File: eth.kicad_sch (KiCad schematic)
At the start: 44 parts, among them J5 Bus_RJ45_5-2337992-8, Q4 DTC014T_SOT-416, Q5 DTC014T_SOT-416, U30 DP83867CR_VQFN, Y6 Oscillator_SMD_25MHz_ECS-2016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

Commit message: [#56935] Update symbol/footprint links; Migrate to KiCad 7
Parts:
- C100, C101, C102, C103, C104, C105, C106, C107, C108, C239, C240, C99: footprint kria-k26-devboard-footprints:C_0402_1005Metric -> antmicro-footprints:C_0402_1005Metric; symbol kria-k26-devboard:C_100n_0402 -> antmicroCapacitors0402:C_100n_0402
- C109, C110, C111, C112, C94, C95, C96, C97, C98: footprint kria-k26-devboard-footprints:C_0402_1005Metric -> antmicro-footprints:C_0402_1005Metric; symbol kria-k26-devboard:C_1u_0402 -> antmicroCapacitors0402:C_1u_0402
- C113, C92, C93: footprint kria-k26-devboard-footprints:C_0402_1005Metric -> antmicro-footprints:C_0402_1005Metric; symbol kria-k26-devboard:C_10n_0402 -> antmicroCapacitors0402:C_10n_0402
- C114, C90, C91: footprint kria-k26-devboard-footprints:C_0603_1608Metric -> antmicro-footprints:C_0603_1608Metric; symbol kria-k26-devboard:C_10u_0603 -> antmicroCapacitors0603:C_10u_0603
- J5: footprint kria-k26-devboard-footprints:RJ45_5-2337992-8_Horizontal -> antmicro-footprints:RJ45_5-2337992-8_Horizontal; symbol kria-k26-devboard:Bus_RJ45_5-2337992-8 -> antmicroModularConnectorsJacksWithMagnetics:Bus_RJ45_5-2337992-8
- Q4, Q5: footprint kria-k26-devboard-footprints:SOT-416 -> antmicro-footprints:SOT-416; symbol kria-k26-devboard:DTC014T_SOT-416 -> antmicroTransistorsBipolarSingle:DTC014T_SOT-416
- R67: footprint kria-k26-devboard-footprints:R_0402_1005Metric -> antmicro-footprints:R_0402_1005Metric; symbol kria-k26-devboard:R_10k_0402 -> antmicroResistors0402:R_10k_0402
- R68, R70: footprint kria-k26-devboard-footprints:R_0402_1005Metric -> antmicro-footprints:R_0402_1005Metric; symbol kria-k26-devboard:R_2k49_0402 -> antmicroResistors0402:R_2k49_0402
- R69: footprint kria-k26-devboard-footprints:R_0402_1005Metric -> antmicro-footprints:R_0402_1005Metric; symbol kria-k26-devboard:R_5k76_0402 -> antmicroResistors0402:R_5k76_0402
- R71, R76: footprint kria-k26-devboard-footprints:R_0402_1005Metric -> antmicro-footprints:R_0402_1005Metric; symbol kria-k26-devboard:R_2k2_0402 -> antmicroResistors0402:R_2k2_0402
- R72: footprint kria-k26-devboard-footprints:R_0402_1005Metric -> antmicro-footprints:R_0402_1005Metric; symbol kria-k26-devboard:R_11k_0402 -> antmicroResistors0402:R_11k_0402
- R73, R74, R75: footprint kria-k26-devboard-footprints:R_0402_1005Metric -> antmicro-footprints:R_0402_1005Metric; symbol kria-k26-devboard:R_4k7_0402 -> antmicroResistors0402:R_4k7_0402
- R77, R78: footprint kria-k26-devboard-footprints:R_0402_1005Metric -> antmicro-footprints:R_0402_1005Metric; symbol kria-k26-devboard:R_330R_0402 -> antmicroResistors0402:R_330R_0402
- U30: footprint kria-k26-devboard-footprints:QFN-48-1EP_7x7mm -> antmicro-footprints:QFN-48-1EP_7x7mm; symbol kria-k26-devboard:DP83867CR_VQFN -> antmicroInterfaceControllers:DP83867CR_VQFN
- Y6: footprint kria-k26-devboard-footprints:Oscillator_SMD_ECS_2016MV_2x1.6x0.85mm -> antmicro-footprints:Oscillator_SMD_ECS_2016MV_2x1.6x0.85mm; symbol kria-k26-devboard:Oscillator_SMD_25MHz_ECS-2016MV -> antmicroOscillators:Oscillator_25MHz_ESC_2016MV

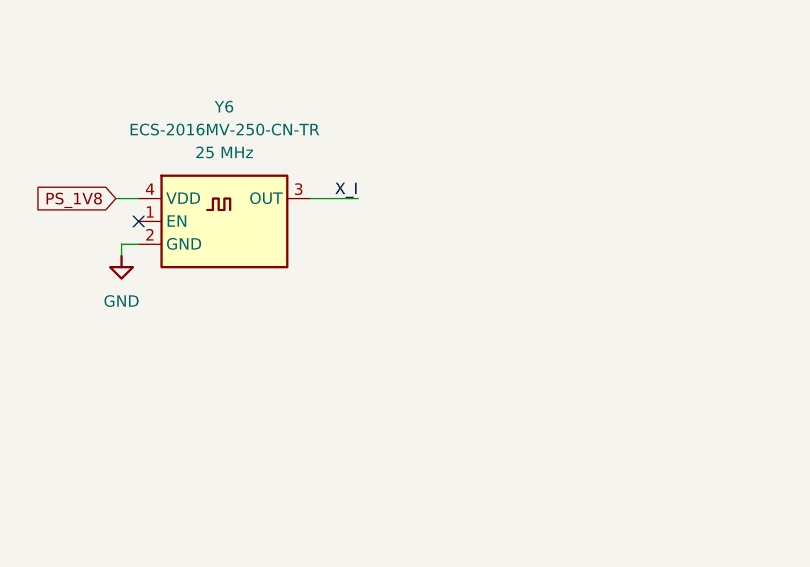
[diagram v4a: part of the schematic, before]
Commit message: [#56935] Fix missing highlights in OHP
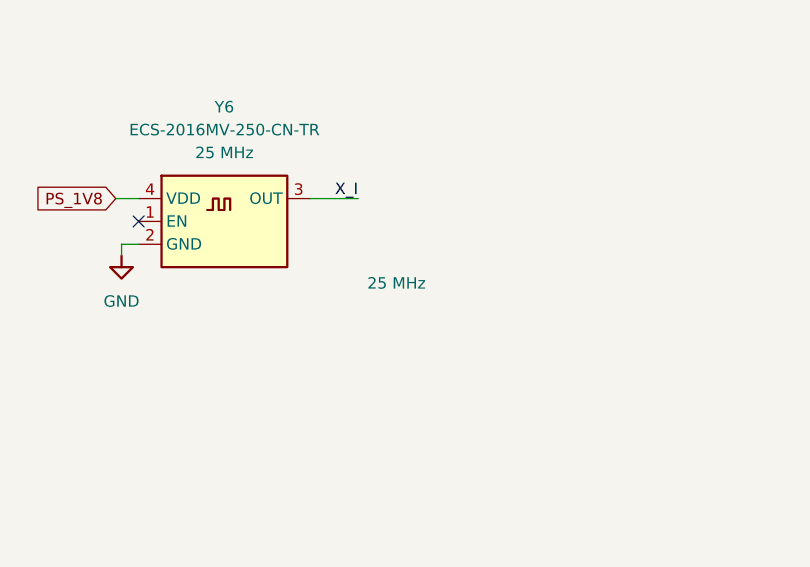
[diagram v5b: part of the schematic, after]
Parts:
- J5: VSD_Class (none) -> Ethernet
- Y6: value Oscillator_SMD_25MHz_ECS-2016MV -> Oscillator_25MHz_ESC_2016MV; Manufacturer ECS Inc. -> ECS Inc. International; Val (none) -> 25 MHz
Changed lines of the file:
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@@
       (effects (font (size 1.27 1.27) (thickness 0.15)) (justify left bottom) hide)
+    )
+    (property "VSD_Class" "Ethernet" (at 285.75 101.6 0)
+      (effects (font (size 1.27 1.27)) (justify left bottom) hide)
     )
     (pin "1")
@@
       (effects (font (size 1.27 1.27)))
     )
-    (property "Value" "Oscillator_SMD_25MHz_ECS-2016MV" (at 122.555 212.725 0)
+    (property "Value" "Oscillator_25MHz_ESC_2016MV" (at 122.555 212.725 0)
       (effects (font (size 1.27 1.27) (thickness 0.15)) hide)
     )
@@
       (effects (font (size 1.27 1.27) (thickness 0.15)) (justify left bottom) hide)
     )
-    (property "Datasheet" "https://www.mouser.pl/datasheet/2/122/ECS_2016MV-2529299.pdf" (at 108.585 217.17 0)
-      (effects (font (size 1.27 1.27) (thickness 0.15)) (justify left bottom) hide)
-    )
-    (property "Manufacturer" "ECS Inc." (at 116.84 231.775 0)
+    (property "Datasheet" "https://ecsxtal.com/store/pdf/ECS-2016MV.pdf" (at 108.585 217.17 0)
+      (effects (font (size 1.27 1.27) (thickness 0.15)) (justify left bottom) hide)
+    )
+    (property "Manufacturer" "ECS Inc. International" (at 116.84 231.775 0)
       (effects (font (size 1.27 1.27) (thickness 0.15)) (justify left bottom) hide)
     )
@@
       (effects (font (size 1.27 1.27) (thickness 0.15)))
     )
-    (pin "1")
+    (property "Val" "25 MHz" (at 138.43 230.505 0)
+      (effects (font (size 1.27 1.27) (thickness 0.15)) (justify left bottom))
+    )
+    (pin "1")

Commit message: [#56935] Loclib
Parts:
- C100, C101, C102, C103, C104, C105, C106, C107, C108, C239, C240, C99: footprint antmicro-footprints:C_0402_1005Metric -> kria-k26-devboard-footprints:C_0402_1005Metric; symbol antmicroCapacitors0402:C_100n_0402 -> kria-k26-devboard:C_100n_0402
- C109, C110, C111, C112, C94, C95, C96, C97, C98: footprint antmicro-footprints:C_0402_1005Metric -> kria-k26-devboard-footprints:C_0402_1005Metric; symbol antmicroCapacitors0402:C_1u_0402 -> kria-k26-devboard:C_1u_0402
- C113, C92, C93: footprint antmicro-footprints:C_0402_1005Metric -> kria-k26-devboard-footprints:C_0402_1005Metric; symbol antmicroCapacitors0402:C_10n_0402 -> kria-k26-devboard:C_10n_0402
- C114, C90, C91: footprint antmicro-footprints:C_0603_1608Metric -> kria-k26-devboard-footprints:C_0603_1608Metric; symbol antmicroCapacitors0603:C_10u_0603 -> kria-k26-devboard:C_10u_0603
- J5: footprint antmicro-footprints:RJ45_5-2337992-8_Horizontal -> kria-k26-devboard-footprints:RJ45_5-2337992-8_Horizontal; symbol antmicroModularConnectorsJacksWithMagnetics:Bus_RJ45_5-2337992-8 -> kria-k26-devboard:Bus_RJ45_5-2337992-8
- Q4, Q5: footprint antmicro-footprints:SOT-416 -> kria-k26-devboard-footprints:SOT-416; symbol antmicroTransistorsBipolarSingle:DTC014T_SOT-416 -> kria-k26-devboard:DTC014T_SOT-416
- R67: footprint antmicro-footprints:R_0402_1005Metric -> kria-k26-devboard-footprints:R_0402_1005Metric; symbol antmicroResistors0402:R_10k_0402 -> kria-k26-devboard:R_10k_0402
- R68, R70: footprint antmicro-footprints:R_0402_1005Metric -> kria-k26-devboard-footprints:R_0402_1005Metric; symbol antmicroResistors0402:R_2k49_0402 -> kria-k26-devboard:R_2k49_0402
- R69: footprint antmicro-footprints:R_0402_1005Metric -> kria-k26-devboard-footprints:R_0402_1005Metric; symbol antmicroResistors0402:R_5k76_0402 -> kria-k26-devboard:R_5k76_0402
- R71, R76: footprint antmicro-footprints:R_0402_1005Metric -> kria-k26-devboard-footprints:R_0402_1005Metric; symbol antmicroResistors0402:R_2k2_0402 -> kria-k26-devboard:R_2k2_0402
- R72: footprint antmicro-footprints:R_0402_1005Metric -> kria-k26-devboard-footprints:R_0402_1005Metric; symbol antmicroResistors0402:R_11k_0402 -> kria-k26-devboard:R_11k_0402
- R73, R74, R75: footprint antmicro-footprints:R_0402_1005Metric -> kria-k26-devboard-footprints:R_0402_1005Metric; symbol antmicroResistors0402:R_4k7_0402 -> kria-k26-devboard:R_4k7_0402
- R77, R78: footprint antmicro-footprints:R_0402_1005Metric -> kria-k26-devboard-footprints:R_0402_1005Metric; symbol antmicroResistors0402:R_330R_0402 -> kria-k26-devboard:R_330R_0402
- U30: footprint antmicro-footprints:QFN-48-1EP_7x7mm -> kria-k26-devboard-footprints:QFN-48-1EP_7x7mm; symbol antmicroInterfaceControllers:DP83867CR_VQFN -> kria-k26-devboard:DP83867CR_VQFN
- Y6: footprint antmicro-footprints:Oscillator_SMD_ECS_2016MV_2x1.6x0.85mm -> kria-k26-devboard-footprints:Oscillator_SMD_ECS_2016MV_2x1.6x0.85mm; symbol antmicroOscillators:Oscillator_25MHz_ESC_2016MV -> kria-k26-devboard:Oscillator_25MHz_ESC_2016MV
